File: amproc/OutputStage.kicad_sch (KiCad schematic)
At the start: 23 parts

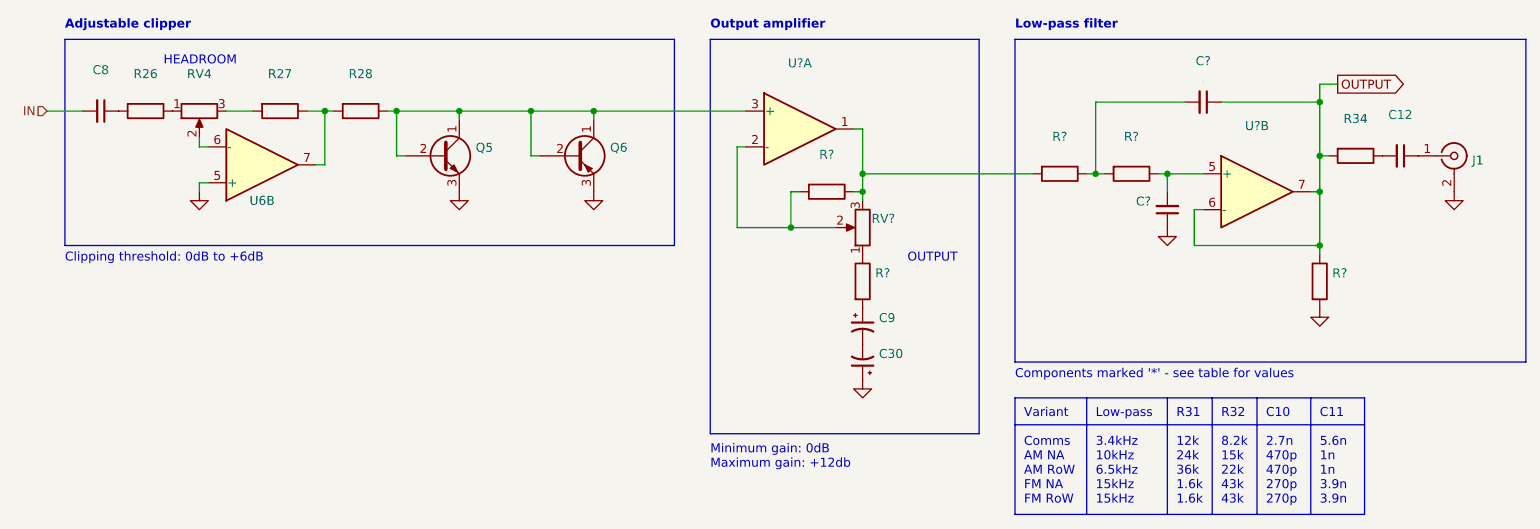
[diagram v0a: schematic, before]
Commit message: Fix U8, U9 pinouts
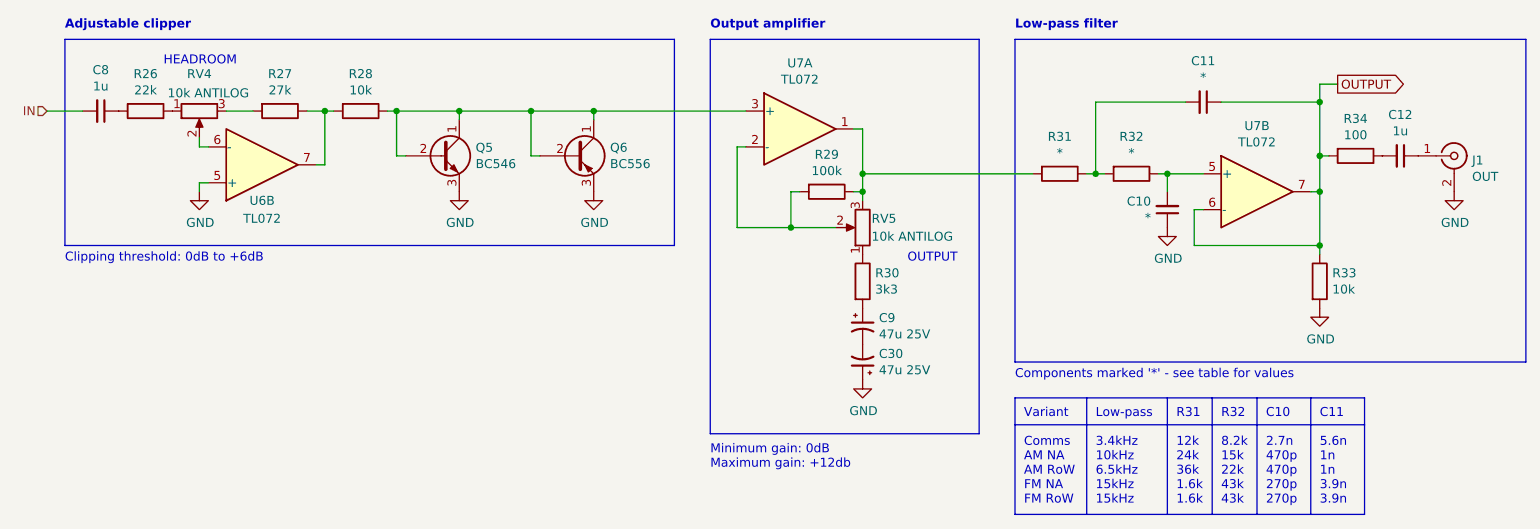
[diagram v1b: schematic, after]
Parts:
- C10, C11: renamed from C?; value (none) -> *; footprint (none) -> Capacitors_THT:C_Rect_L7.2mm_W2.5mm_P5.00mm_FKS2_FKP2_MKS2_MKP2
- C12, C8: value (none) -> 1u; footprint (none) -> Capacitors_THT:C_Rect_L7.2mm_W5.5mm_P5.00mm_FKS2_FKP2_MKS2_MKP2
- C30, C9: value (none) -> 47u 25V; footprint (none) -> Capacitors_THT:CP_Radial_D5.0mm_P2.00mm
- J1: value (none) -> OUT; footprint (none) -> amproc:NYS354
- Q5: value (none) -> BC546; footprint (none) -> TO_SOT_Packages_THT:TO-92_Inline_Narrow_Oval
- Q6: value (none) -> BC556; footprint (none) -> TO_SOT_Packages_THT:TO-92_Inline_Narrow_Oval
- R26: value (none) -> 22k; footprint (none) -> amproc:R_Axial_DIN0207_L6.3mm_D2.5mm_P7.62mm_Horizontal_FabText
- R27: value (none) -> 27k; footprint (none) -> amproc:R_Axial_DIN0207_L6.3mm_D2.5mm_P7.62mm_Horizontal_FabText
- R28: value (none) -> 10k; footprint (none) -> amproc:R_Axial_DIN0207_L6.3mm_D2.5mm_P7.62mm_Horizontal_FabText
- R29: renamed from R?; value (none) -> 100k; footprint (none) -> amproc:R_Axial_DIN0207_L6.3mm_D2.5mm_P7.62mm_Horizontal_FabText
- R30: renamed from R?; value (none) -> 3k3; footprint (none) -> amproc:R_Axial_DIN0207_L6.3mm_D2.5mm_P7.62mm_Horizontal_FabText
- R31, R32: renamed from R?; value (none) -> *; footprint (none) -> amproc:R_Axial_DIN0207_L6.3mm_D2.5mm_P7.62mm_Horizontal_FabText
- R33: renamed from R?; value (none) -> 10k; footprint (none) -> amproc:R_Axial_DIN0207_L6.3mm_D2.5mm_P7.62mm_Horizontal_FabText
- R34: value (none) -> 100; footprint (none) -> amproc:R_Axial_DIN0207_L6.3mm_D2.5mm_P7.62mm_Horizontal_FabText
- RV4: value (none) -> 10k ANTILOG; footprint (none) -> amproc:PTD901-15K
- RV5: renamed from RV?; value (none) -> 10k ANTILOG; footprint (none) -> amproc:PTD901-15K
- U6: value (none) -> TL072; footprint (none) -> Housings_DIP:DIP-8_W7.62mm_LongPads
- U7: renamed from U?; value (none) -> TL072; footprint (none) -> Housings_DIP:DIP-8_W7.62mm_LongPads
